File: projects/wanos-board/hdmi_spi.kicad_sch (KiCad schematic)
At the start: 2 parts, among them J1 HDMI_EINK

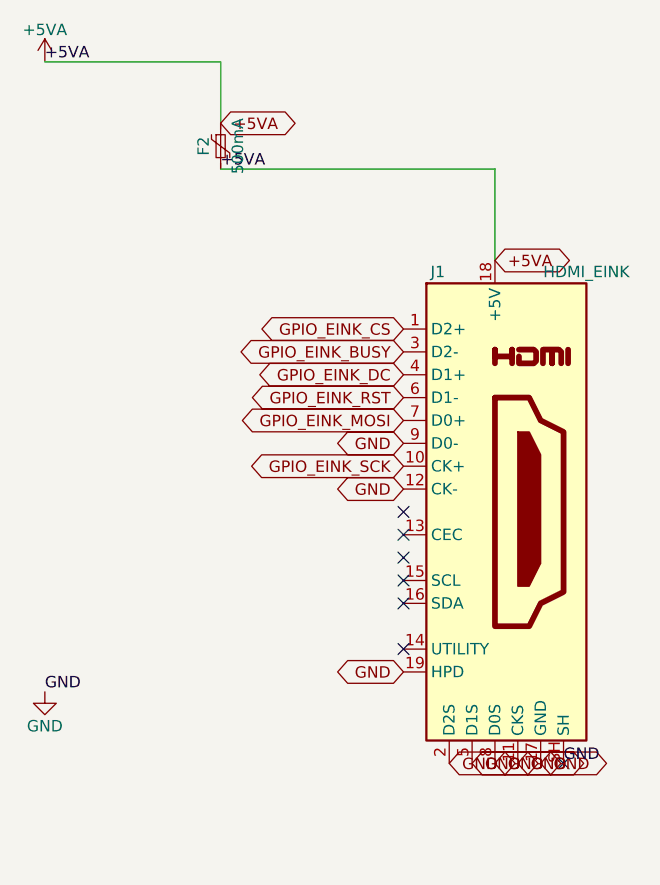
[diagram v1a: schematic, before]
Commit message: SSR, power, IO_expander schemas update
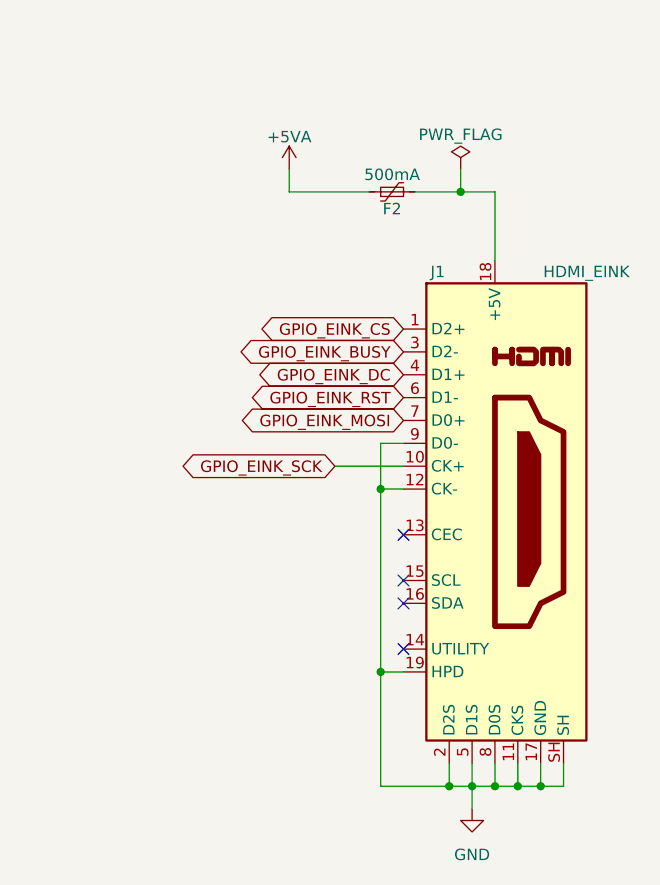
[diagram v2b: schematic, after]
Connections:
- net +5VA: no longer F2.2, J1.18 (+5V)
- new net: F2.2, J1.18 (+5V)
- no-connect marks 7 -> 4
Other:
- moved on the sheet: F2
